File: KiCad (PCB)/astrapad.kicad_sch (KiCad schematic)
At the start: 34 parts, among them J1 OLED_DISPLAY, SW1 SW_Push, SW13 RotaryEncoder_Switch, SW2 SW_Push, SW3 SW_Push, SW5 SW_Push, SW6 SW_Push, SW7 SW_Push, SW8 SW_Push, U1 XIAO-RP2040-DIP

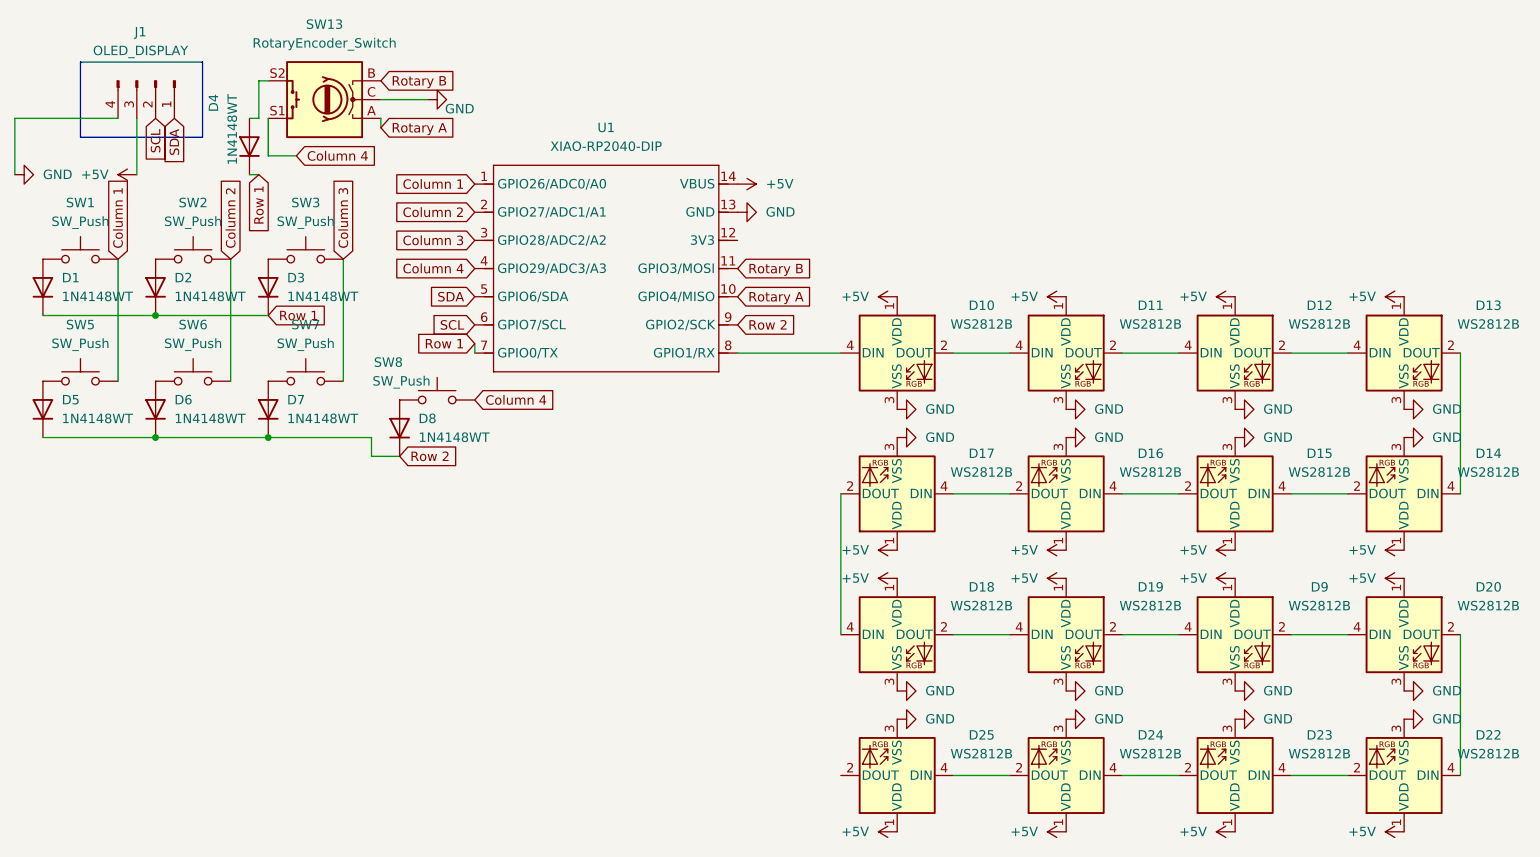
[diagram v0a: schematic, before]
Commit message: Some PCB Rerouting And by "some", I mean all of it. I didn't account for the size of the actual OLED screen (just had the pins before), so I had to reroute basically everything once I did.
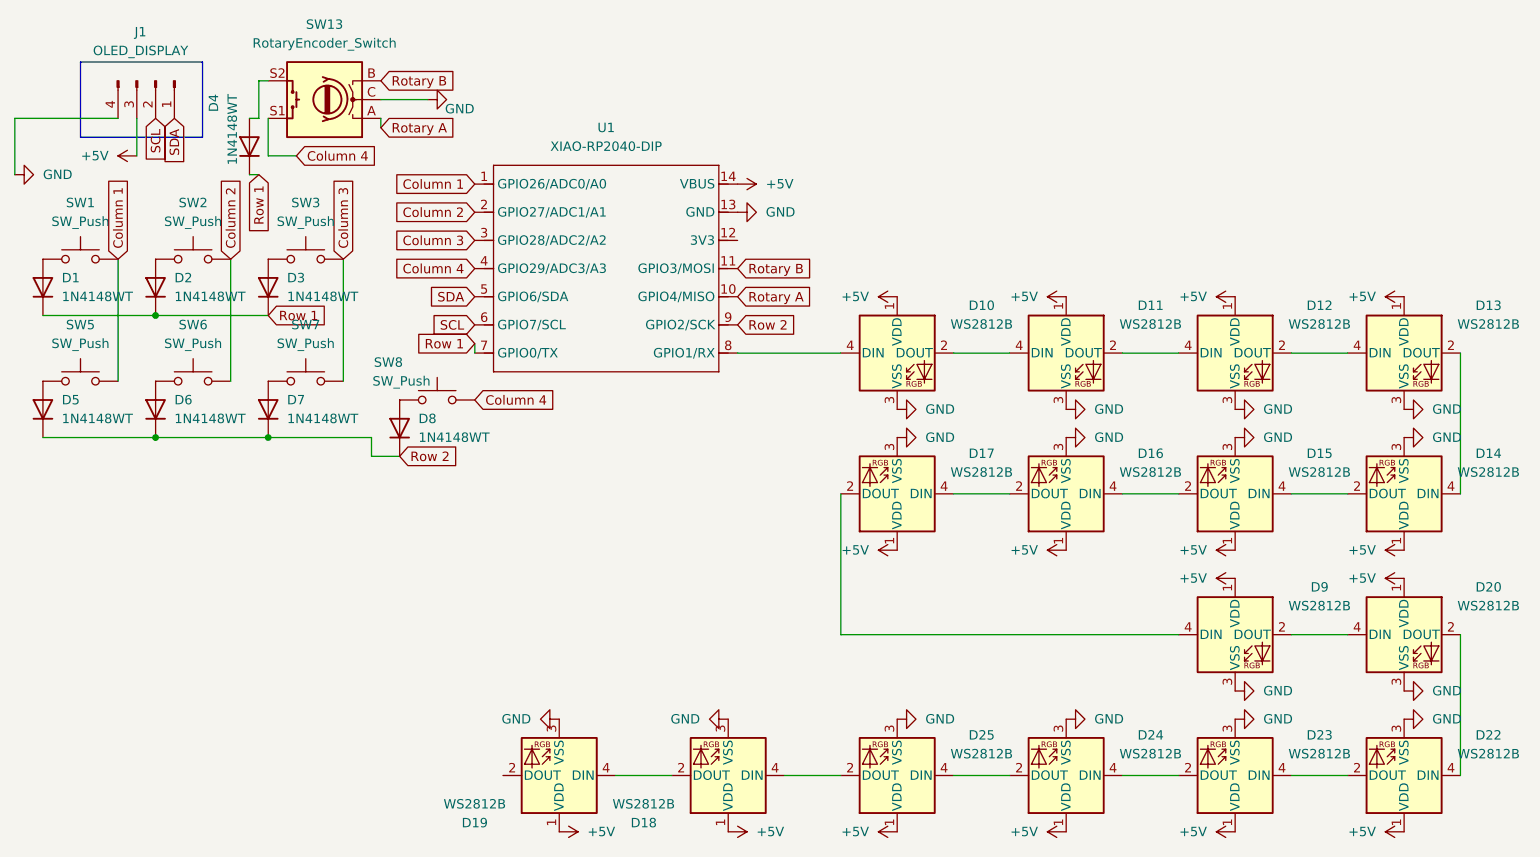
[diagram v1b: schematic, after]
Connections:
- net at D25.2 (DOUT): now also D18.4 (DIN)
- net at D19.2 (DOUT): no longer D9.4 (DIN)
- net at D17.2 (DOUT): now also D9.4 (DIN); no longer D18.4 (DIN)
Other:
- moved on the sheet: D18, D19
